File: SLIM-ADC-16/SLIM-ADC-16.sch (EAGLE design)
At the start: 34 parts, among them J1 COAX, J2 COAX, P1 CONN-6PIN, Q1 MUN2211, Q2 MUN2211, SW1 SPDT-CONN, SW2 SPDT-CONN, U1 78L05, U2 AD7685, U3 AD7685

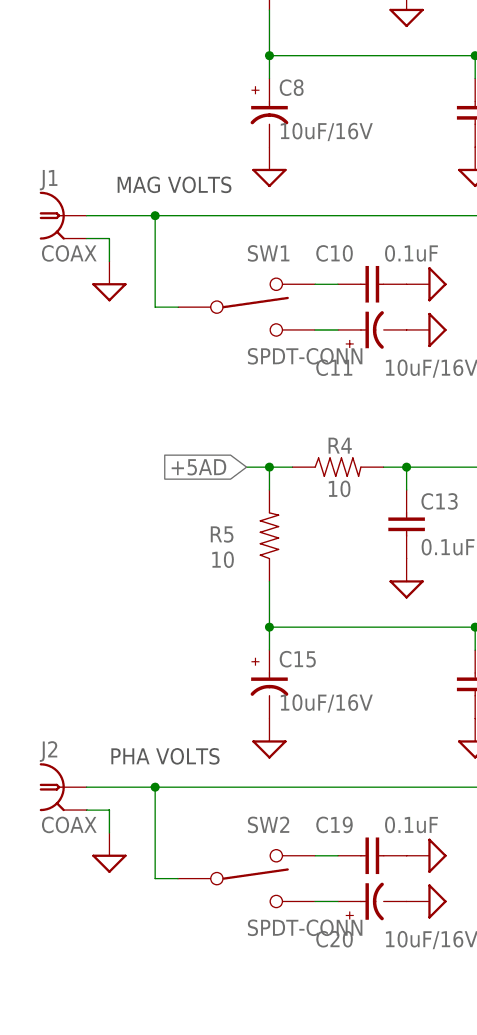
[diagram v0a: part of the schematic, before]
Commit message: Fixup the coax symbol to automatically connect the ground Add the DDS board Add a design rules file, based on the BatchPCB specs.
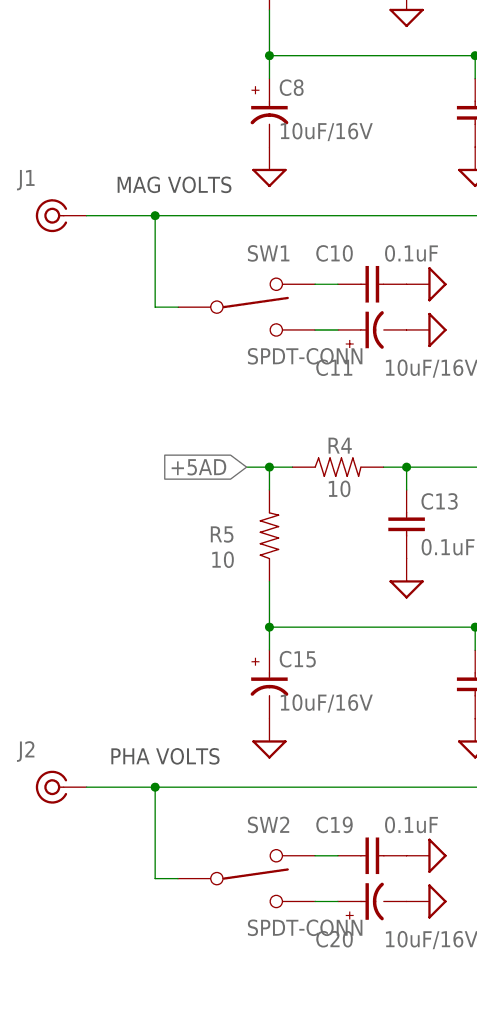
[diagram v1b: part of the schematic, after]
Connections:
- net GND: no longer J1.GND, J2.GND
- net N$10: now also J2G$1.1; no longer J2.1
- net N$3: now also J1G$1.1; no longer J1.1
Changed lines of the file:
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@@
 <grid distance="0.1" unitdist="inch" unit="inch" style="lines" multiple="1" display="no" altdistance="0.01" altunitdist="inch" altunit="inch"/>
 <layers>
-<layer number="1" name="Top" color="4" fill="1" visible="yes" active="no"/>
-<layer number="2" name="Route2" color="1" fill="3" visible="yes" active="no"/>
-<layer number="15" name="Route15" color="4" fill="6" visible="yes" active="no"/>
-<layer number="16" name="Bottom" color="1" fill="1" visible="yes" active="no"/>
-<layer number="17" name="Pads" color="2" fill="1" visible="yes" active="no"/>
-<layer number="18" name="Vias" color="2" fill="1" visible="yes" active="no"/>
-<layer number="19" name="Unrouted" color="6" fill="1" visible="yes" active="no"/>
-<layer number="20" name="Dimension" color="15" fill="1" visible="yes" active="no"/>
-<layer number="21" name="tPlace" color="16" fill="1" visible="yes" active="no"/>
-<layer number="22" name="bPlace" color="14" fill="1" visible="yes" active="no"/>
-<layer number="23" name="tOrigins" color="15" fill="1" visible="yes" active="no"/>
-<layer number="24" name="bOrigins" color="15" fill="1" visible="yes" active="no"/>
-<layer number="25" name="tNames" color="16" fill="1" visible="yes" active="no"/>
-<layer number="26" name="bNames" color="7" fill="1" visible="yes" active="no"/>
-<layer number="27" name="tValues" color="7" fill="1" visible="yes" active="no"/>
-<layer number="28" name="bValues" color="7" fill="1" visible="yes" active="no"/>
+<layer number="1" name="Top" color="4" fill="1" visible="no" active="no"/>
+<layer number="2" name="Route2" color="1" fill="3" visible="no" active="no"/>
+<layer number="15" name="Route15" color="4" fill="6" visible="no" active="no"/>
+<layer number="16" name="Bottom" color="1" fill="1" visible="no" active="no"/>
+<layer number="17" name="Pads" color="2" fill="1" visible="no" active="no"/>
+<layer number="18" name="Vias" color="2" fill="1" visible="no" active="no"/>
+<layer number="19" name="Unrouted" color="6" fill="1" visible="no" active="no"/>
+<layer number="20" name="Dimension" color="15" fill="1" visible="no" active="no"/>
+<layer number="21" name="tPlace" color="16" fill="1" visible="no" active="no"/>
+<layer number="22" name="bPlace" color="14" fill="1" visible="no" active="no"/>
+<layer number="23" name="tOrigins" color="15" fill="1" visible="no" active="no"/>
+<layer number="24" name="bOrigins" color="15" fill="1" visible="no" active="no"/>
+<layer number="25" name="tNames" color="16" fill="1" visible="no" active="no"/>
+<layer number="26" name="bNames" color="7" fill="1" visible="no" active="no"/>
+<layer number="27" name="tValues" color="7" fill="1" visible="no" active="no"/>
+<layer number="28" name="bValues" color="7" fill="1" visible="no" active="no"/>
 <layer number="29" name="tStop" color="7" fill="3" visible="no" active="no"/>
 <layer number="30" name="bStop" color="7" fill="6" visible="no" active="no"/>
@@
 <layer number="35" name="tGlue" color="7" fill="4" visible="no" active="no"/>
 <layer number="36" name="bGlue" color="7" fill="5" visible="no" active="no"/>
-<layer number="37" name="tTest" color="7" fill="1" visible="yes" active="no"/>
-<layer number="38" name="bTest" color="7" fill="1" visible="yes" active="no"/>
+<layer number="37" name="tTest" color="7" fill="1" visible="no" active="no"/>
+<layer number="38" name="bTest" color="7" fill="1" visible="no" active="no"/>
 <layer number="39" name="tKeepout" color="4" fill="11" visible="no" active="no"/>
 <layer number="40" name="bKeepout" color="1" fill="11" visible="no" active="no"/>
@@
 <layer number="44" name="Drills" color="7" fill="1" visible="no" active="no"/>
 <layer number="45" name="Holes" color="7" fill="1" visible="no" active="no"/>
-<layer number="46" name="Milling" color="3" fill="1" visible="yes" active="no"/>
-<layer number="47" name="Measures" color="7" fill="1" visible="yes" active="no"/>
-<layer number="48" name="Document" color="7" fill="1" visible="yes" active="no"/>
-<layer number="49" name="Reference" color="7" fill="1" visible="yes" active="no"/>
-<layer number="50" name="dxf" color="7" fill="1" visible="yes" active="no"/>
-<layer number="51" name="tDocu" color="6" fill="1" visible="yes" active="no"/>
-<layer number="52" name="bDocu" color="7" fill="1" visible="yes" active="no"/>
-<layer number="53" name="tGND_GNDA" color="7" fill="9" visible="yes" active="no"/>
-<layer number="54" name="bGND_GNDA" color="1" fill="9" visible="yes" active="no"/>
-<layer number="56" name="wert" color="7" fill="1" visible="yes" active="no"/>
+<layer number="46" name="Milling" color="3" fill="1" visible="no" active="no"/>
+<layer number="47" name="Measures" color="7" fill="1" visible="no" active="no"/>
+<layer number="48" name="Document" color="7" fill="1" visible="no" active="no"/>
+<layer number="49" name="Reference" color="7" fill="1" visible="no" active="no"/>
+<layer number="50" name="dxf" color="7" fill="1" visible="no" active="no"/>
+<layer number="51" name="tDocu" color="6" fill="1" visible="no" active="no"/>
+<layer number="52" name="bDocu" color="7" fill="1" visible="no" active="no"/>
+<layer number="53" name="tGND_GNDA" color="7" fill="9" visible="no" active="no"/>
+<layer number="54" name="bGND_GNDA" color="1" fill="9" visible="no" active="no"/>
+<layer number="56" name="wert" color="7" fill="1" visible="no" active="no"/>
 <layer number="91" name="Nets" color="2" fill="1" visible="yes" active="yes"/>
 <layer number="92" name="Busses" color="1" fill="1" visible="yes" active="yes"/>
@@
 <part name="GND6" library="SLIM" deviceset="GND" device=""/>
 <part name="J1" library="SLIM" deviceset="COAX" device=""/>
-<part name="GND7" library="SLIM" deviceset="GND" device=""/>
 <part name="C10" library="SLIM" deviceset="CAP" device="0805" value="0.1uF"/>
 <part name="C11" library="SLIM" deviceset="CAP-POL" device="1206" value="10uF/16V"/>
@@
 <part name="GND24" library="SLIM" deviceset="GND" device=""/>
 <part name="J2" library="SLIM" deviceset="COAX" device=""/>
-<part name="GND25" library="SLIM" deviceset="GND" device=""/>
 <part name="C19" library="SLIM" deviceset="CAP" device="0805" value="0.1uF"/>
 <part name="C20" library="SLIM" deviceset="CAP-POL" device="1206" value="10uF/16V"/>
@@
 <instance part="GND6" gate="1" x="119.38" y="109.22"/>
 <instance part="J1" gate="G$1" x="48.26" y="119.38"/>
-<instance part="GND7" gate="1" x="53.34" y="111.76"/>
 <instance part="C10" gate="G$1" x="83.82" y="111.76" smashed="yes" rot="R90">
 <attribute name="NAME" x="76.2" y="114.3" size="1.778" layer="95"/>
@@
 <instance part="GND24" gate="1" x="119.38" y="45.72"/>
 <instance part="J2" gate="G$1" x="48.26" y="55.88"/>
-<instance part="GND25" gate="1" x="53.34" y="48.26"/>
 <instance part="C19" gate="G$1" x="83.82" y="48.26" smashed="yes" rot="R90">
 <attribute name="NAME" x="76.2" y="50.8" size="1.778" layer="95"/>
@@
 </segment>
 <segment>
-<pinref part="J1" gate="G$1" pin="GND"/>
-<pinref part="GND7" gate="1" pin="GND"/>
-<wire x1="50.8" y1="116.84" x2="53.34" y2="116.84" width="0.1524" layer="91"/>
-<wire x1="53.34" y1="116.84" x2="53.34" y2="114.3" width="0.1524" layer="91"/>
-</segment>
-<segment>
 <pinref part="C10" gate="G$1" pin="2"/>
 <pinref part="GND9" gate="1" pin="GND"/>
@@
 </segment>
 <segment>
-<pinref part="J2" gate="G$1" pin="GND"/>
-<pinref part="GND25" gate="1" pin="GND"/>
-<wire x1="50.8" y1="53.34" x2="53.34" y2="53.34" width="0.1524" layer="91"/>
-<wire x1="53.34" y1="53.34" x2="53.34" y2="50.8" width="0.1524" layer="91"/>
-</segment>
-<segment>
